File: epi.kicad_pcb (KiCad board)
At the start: 2 copper layers, 12.5 x 23 mm, 28 parts, among them J1 Conn_01x12, J2 Conn_01x12, J3 Conn_01x04, J4 USB_C_Receptacle_USB2.0, U1 ATmega32U4-M, Y1 16mhz

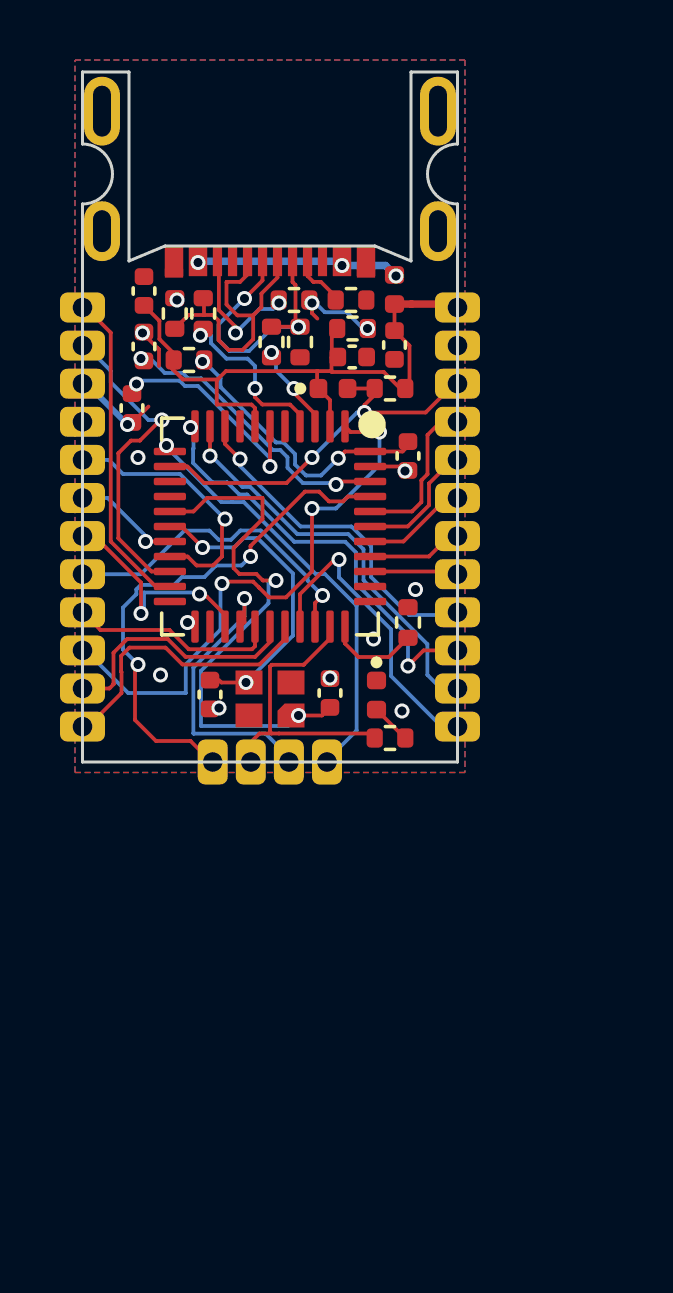
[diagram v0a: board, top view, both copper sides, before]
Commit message: fixed small USB port inaccuracy
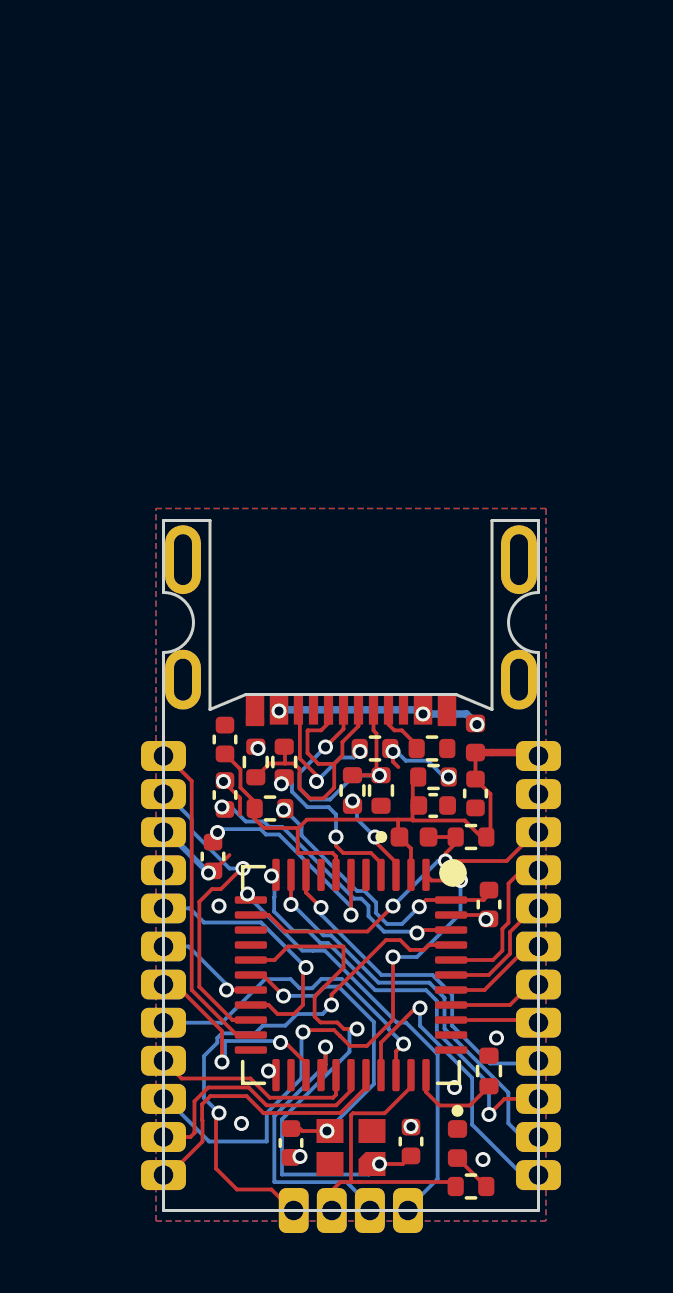
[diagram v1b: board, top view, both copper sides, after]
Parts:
- moved D2 15.2 mm to (106.2, 72.1)
- moved C1 15.2 mm to (105.4, 60.9)
- moved C2 15.2 mm to (107.3, 64.2)
- moved C7 15.2 mm to (98.5, 60.5)
- moved FB1 15.2 mm to (100.0, 61.0)
- moved J1 15.2 mm to (96.5, 59.2)
- moved J2 15.2 mm to (109.0, 59.2)
- moved J4 15.2 mm to (102.7, 53.7)
- moved R2 15.2 mm to (102.8, 60.4)
- moved R4 15.2 mm to (103.5, 59.0)
- moved R5 15.2 mm to (105.4, 59.0)
- moved R7 15.2 mm to (107.3, 69.7)
- moved RV1 15.2 mm to (103.7, 60.4)
- moved U1 15.2 mm to (102.7, 66.5)
- moved Y1 15.2 mm to (102.7, 72.2)
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
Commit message: more descriptive part names and better BOM
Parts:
- D1: value D_Small -> Diode
- D2: value LED_Small -> LED
- F1: value Polyfuse_500mA -> Polyfuse 500mA HC
- FB1: value MH2029-300Y -> Ferrite bead low-pass filter
- J1, J2: value Conn_01x12 -> Connector 1x12
- J3: value Conn_01x04 -> Connector 1x04
- J4: value USB_C_Receptacle_USB2.0 -> USB-C 2.0 mid-mount female connector
- R4, R5: value 56kΩ -> 5,1kΩ
- RV1, RV2: value Varistor -> ESD protection varistor
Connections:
- Y1 pad 3: GND -> (no net)
- Y1 pad 4: GND -> (no net)
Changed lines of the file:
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@@
       (effects (font (size 1 1) (thickness 0.15)))
     )
-    (fp_text value "Varistor" (at 0 1.17 90) (layer "F.Fab")
+    (fp_text value "ESD protection varistor" (at 0 1.17 90) (layer "F.Fab")
       (effects (font (size 1 1) (thickness 0.15)))
     )
@@
       (effects (font (size 1 1) (thickness 0.15)))
     )
-    (fp_text value "56kΩ" (at 0 1.17) (layer "F.Fab")
+    (fp_text value "5,1kΩ" (at 0 1.17) (layer "F.Fab")
       (effects (font (size 1 1) (thickness 0.15)))
     )
@@
       (effects (font (size 1 1) (thickness 0.15)))
     )
-    (fp_text value "LED_Small" (at 0 1.17 90) (layer "F.Fab")
+    (fp_text value "LED" (at 0 1.17 90) (layer "F.Fab")
       (effects (font (size 1 1) (thickness 0.15)))
     )
@@
       (effects (font (size 1 1) (thickness 0.15)))
     )
-    (fp_text value "Conn_01x04" (at 0 5.505 90) (layer "F.Fab")
+    (fp_text value "Connector 1x04" (at 0 5.505 90) (layer "F.Fab")
       (effects (font (size 1 1) (thickness 0.15)))
     )
@@
       (effects (font (size 1 1) (thickness 0.15)))
     )
-    (fp_text value "MH2029-300Y" (at 0 1.17) (layer "F.Fab")
+    (fp_text value "Ferrite bead low-pass filter" (at 0 1.17) (layer "F.Fab")
       (effects (font (size 1 1) (thickness 0.15)))
     )
@@
       (effects (font (size 1 1) (thickness 0.15)))
     )
-    (fp_text value "Varistor" (at 0 1.17 90) (layer "F.Fab")
+    (fp_text value "ESD protection varistor" (at 0 1.17 90) (layer "F.Fab")
       (effects (font (size 1 1) (thickness 0.15)))
     )
@@
       (effects (font (size 1 1) (thickness 0.15)))
     )
-    (fp_text value "D_Small" (at 0 1.17) (layer "F.Fab")
+    (fp_text value "Diode" (at 0 1.17) (layer "F.Fab")
       (effects (font (size 1 1) (thickness 0.15)))
     )
@@
       (effects (font (size 1 1) (thickness 0.15)))
     )
-    (fp_text value "Conn_01x12" (at 0 15.665) (layer "F.Fab")
+    (fp_text value "Connector 1x12" (at 0 15.665) (layer "F.Fab")
       (effects (font (size 1 1) (thickness 0.15)))
     )
@@
     (pad "2" smd rect (at -0.7 -0.55) (size 0.9 0.8) (layers "F.Cu" "F.Paste" "F.Mask")
       (net 4 "Net-(C5-Pad2)") (pinfunction "2") (pintype "passive"))
-    (pad "3" smd rect (at -0.7 0.55) (size 0.9 0.8) (layers "F.Cu" "F.Paste" "F.Mask")
-      (net 2 "GND"))
-    (pad "4" smd rect (at 0.7 -0.55) (size 0.9 0.8) (layers "F.Cu" "F.Paste" "F.Mask")
-      (net 2 "GND"))
+    (pad "3" smd rect (at -0.7 0.55) (size 0.9 0.8) (layers "F.Cu" "F.Paste" "F.Mask"))
+    (pad "4" smd rect (at 0.7 -0.55) (size 0.9 0.8) (layers "F.Cu" "F.Paste" "F.Mask"))
     (zone (net 0) (net_name "") (layer "F.Cu") (hatch edge 0.508)
       (connect_pads (clearance 0.508))
@@
       (effects (font (size 1 1) (thickness 0.15)))
     )
-    (fp_text value "USB_C_Receptacle_USB2.0" (at 0 -7.4 180 unlocked) (layer "F.Fab")
+    (fp_text value "USB-C 2.0 mid-mount female connector" (at 0 -7.4 180 unlocked) (layer "F.Fab")
       (effects (font (size 1 1) (thickness 0.15)))
     )
@@
       (effects (font (size 1 1) (thickness 0.15)))
     )
-    (fp_text value "56kΩ" (at 0 1.17) (layer "F.Fab")
+    (fp_text value "5,1kΩ" (at 0 1.17) (layer "F.Fab")
       (effects (font (size 1 1) (thickness 0.15)))
     )
@@
       (effects (font (size 1 1) (thickness 0.15)))
     )
-    (fp_text value "Polyfuse_500mA" (at 0 1.17 90) (layer "F.Fab")
+    (fp_text value "Polyfuse 500mA HC" (at 0 1.17 90) (layer "F.Fab")
       (effects (font (size 1 1) (thickness 0.15)))
     )
@@
       (effects (font (size 1 1) (thickness 0.15)))
     )
-    (fp_text value "Conn_01x12" (at 0 15.665) (layer "F.Fab")
-      (effects (font (size 1 1) (thickness 0.15)))
-    )
+    (fp_text value "Connector 1x12" (at 0 15.665) (layer "F.Fab")
+      (effects (font (size 1 1) (thickness 0.15)))
+    )

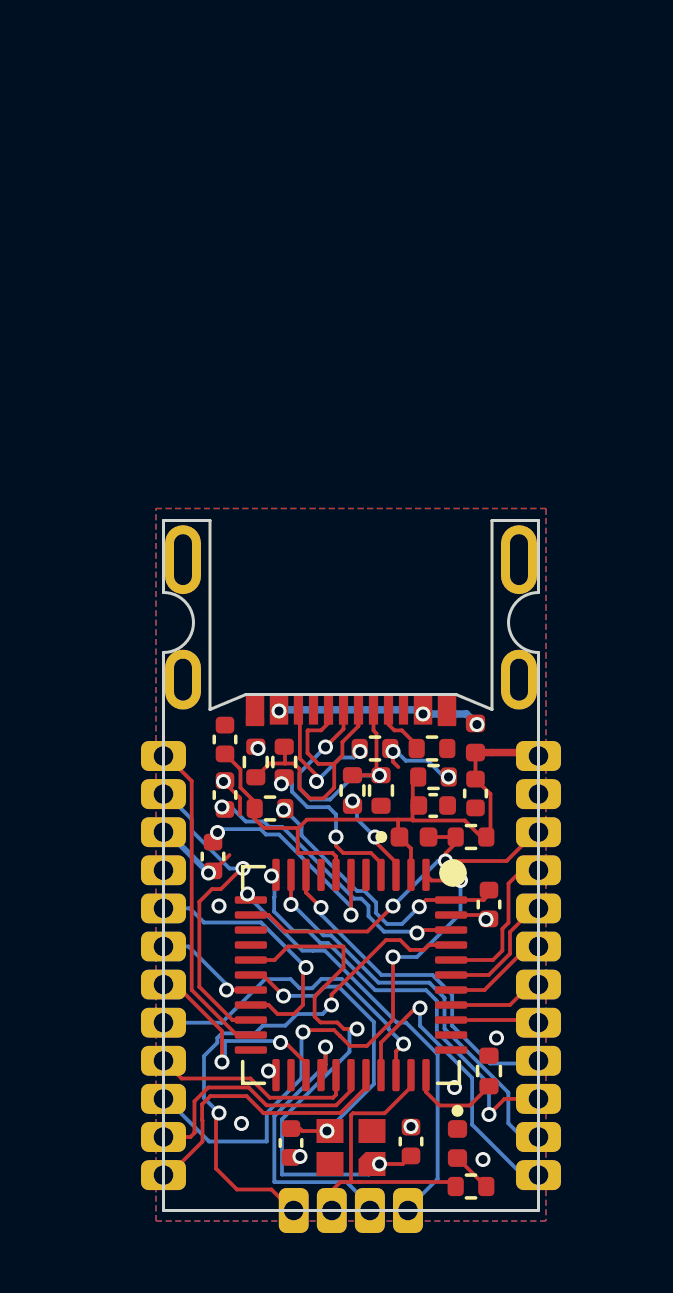
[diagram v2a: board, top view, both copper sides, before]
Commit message: increased trace spacing and a few other changes
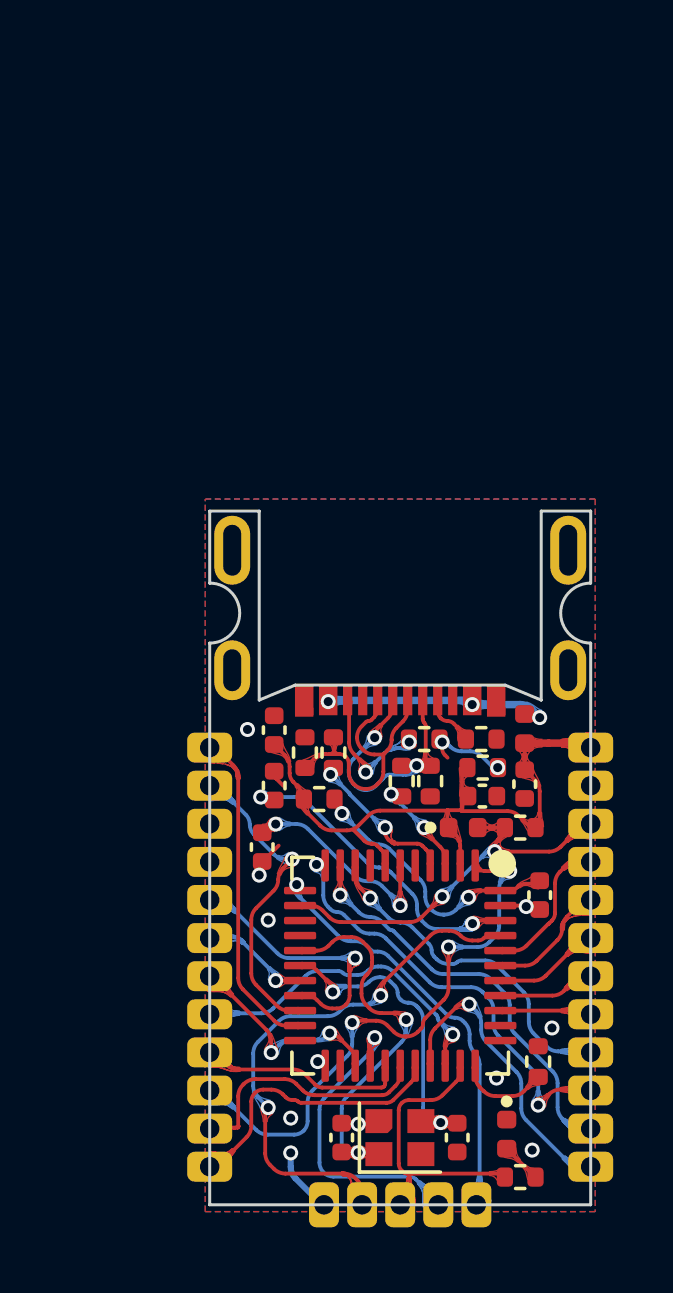
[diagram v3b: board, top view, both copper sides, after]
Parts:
- J3: value Connector 1x04 -> Conn_01x05; footprint Connector_PinHeader_1.27mm:PinHeader_1x04_P1.27mm_Vertical -> Connector_PinHeader_1.27mm:PinHeader_1x05_P1.27mm_Vertical
- Y1: value 16mhz -> Crystal_GND24_Small
- moved C5 5.54 mm to (106.2, 71.9)
- moved C6 2.31 mm to (102.4, 71.9)
- moved J3 2.29 mm to (106.9, 74.2)
- moved J2 1.76 mm to (110.7, 58.9)
- moved C2 1.72 mm to (109.0, 63.8)
- moved C1 1.67 mm to (107.1, 60.5)
- moved C4 1.67 mm to (108.5, 60.1)
- moved D2 1.67 mm to (107.9, 71.8)
- moved F1 1.67 mm to (108.5, 58.3)
- moved FB1 1.67 mm to (101.6, 60.6)
- moved R2 1.67 mm to (104.4, 60.0)
- moved R4 1.67 mm to (105.1, 58.6)
- moved R5 1.67 mm to (107.0, 58.6)
- moved R7 1.67 mm to (108.9, 69.4)
- moved RV1 1.67 mm to (105.3, 60.0)
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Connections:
- Y1 pad 2: Net-(C5-Pad2) -> GND
- Y1 pad 3: (no net) -> Net-(C5-Pad2)
- Y1 pad 4: (no net) -> GND
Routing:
- net Net-(C6-Pad2): track 18.2 -> 13.1 mm
- net VBUS: track 22.0 -> 21.0 mm
- net D4: track 7.70 -> 6.86 mm
- net D+: track 5.83 -> 5.16 mm
- net Net-(C2-Pad2): track 9.23 -> 8.57 mm
- net IO12: track 9.82 -> 10.5 mm
- net A5: track 17.5 -> 18.1 mm
- net Net-(C7-Pad1): track 9.55 -> 10.1 mm
- net GND: track 8.07 -> 8.31 mm, vias 14 -> 13
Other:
- board size 12.5 x 23 mm -> 12.7 x 23.1 mm
- board text added: "Epi v1,2"
- board text removed: "Epi v1,1"
